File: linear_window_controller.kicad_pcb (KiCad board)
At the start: 4 copper layers, 114.3 x 86.4 mm, 148 parts, among them J1 Motor 2, J2 Motor 1, J3 Motor 4, J4 Motor 3, J5 Amphenol 10053363-200LF, J6 ATX-24 (Molex 39-28-1243), J7 Link-PP_LPJ0135GDNL, J8 EXT_LED, J9 Control, P1 ESP32 USB, P2 ESP32 USB, Q1 BC817-40(SOT23), Q2 BC817-40(SOT23), Q3 BSS138, SW1 PGM, SW2 Service, SW3 Service, SW4 Service, SW5 Service, SW7 Service, U1 TSOP384xx, U10 TPS56220x, U11 CP2102N-A01-GQFN24, U12 93LCxxAxxOT, U13 DM9051, U2 DRV8874, U3 DRV8874, U4 DRV8874, U5 DRV8874, U6 PCF8574APWRG4, U8 ESP32-S3-WROOM-1-N16R2, Y1 25MHz YXC X322525MOB4SI

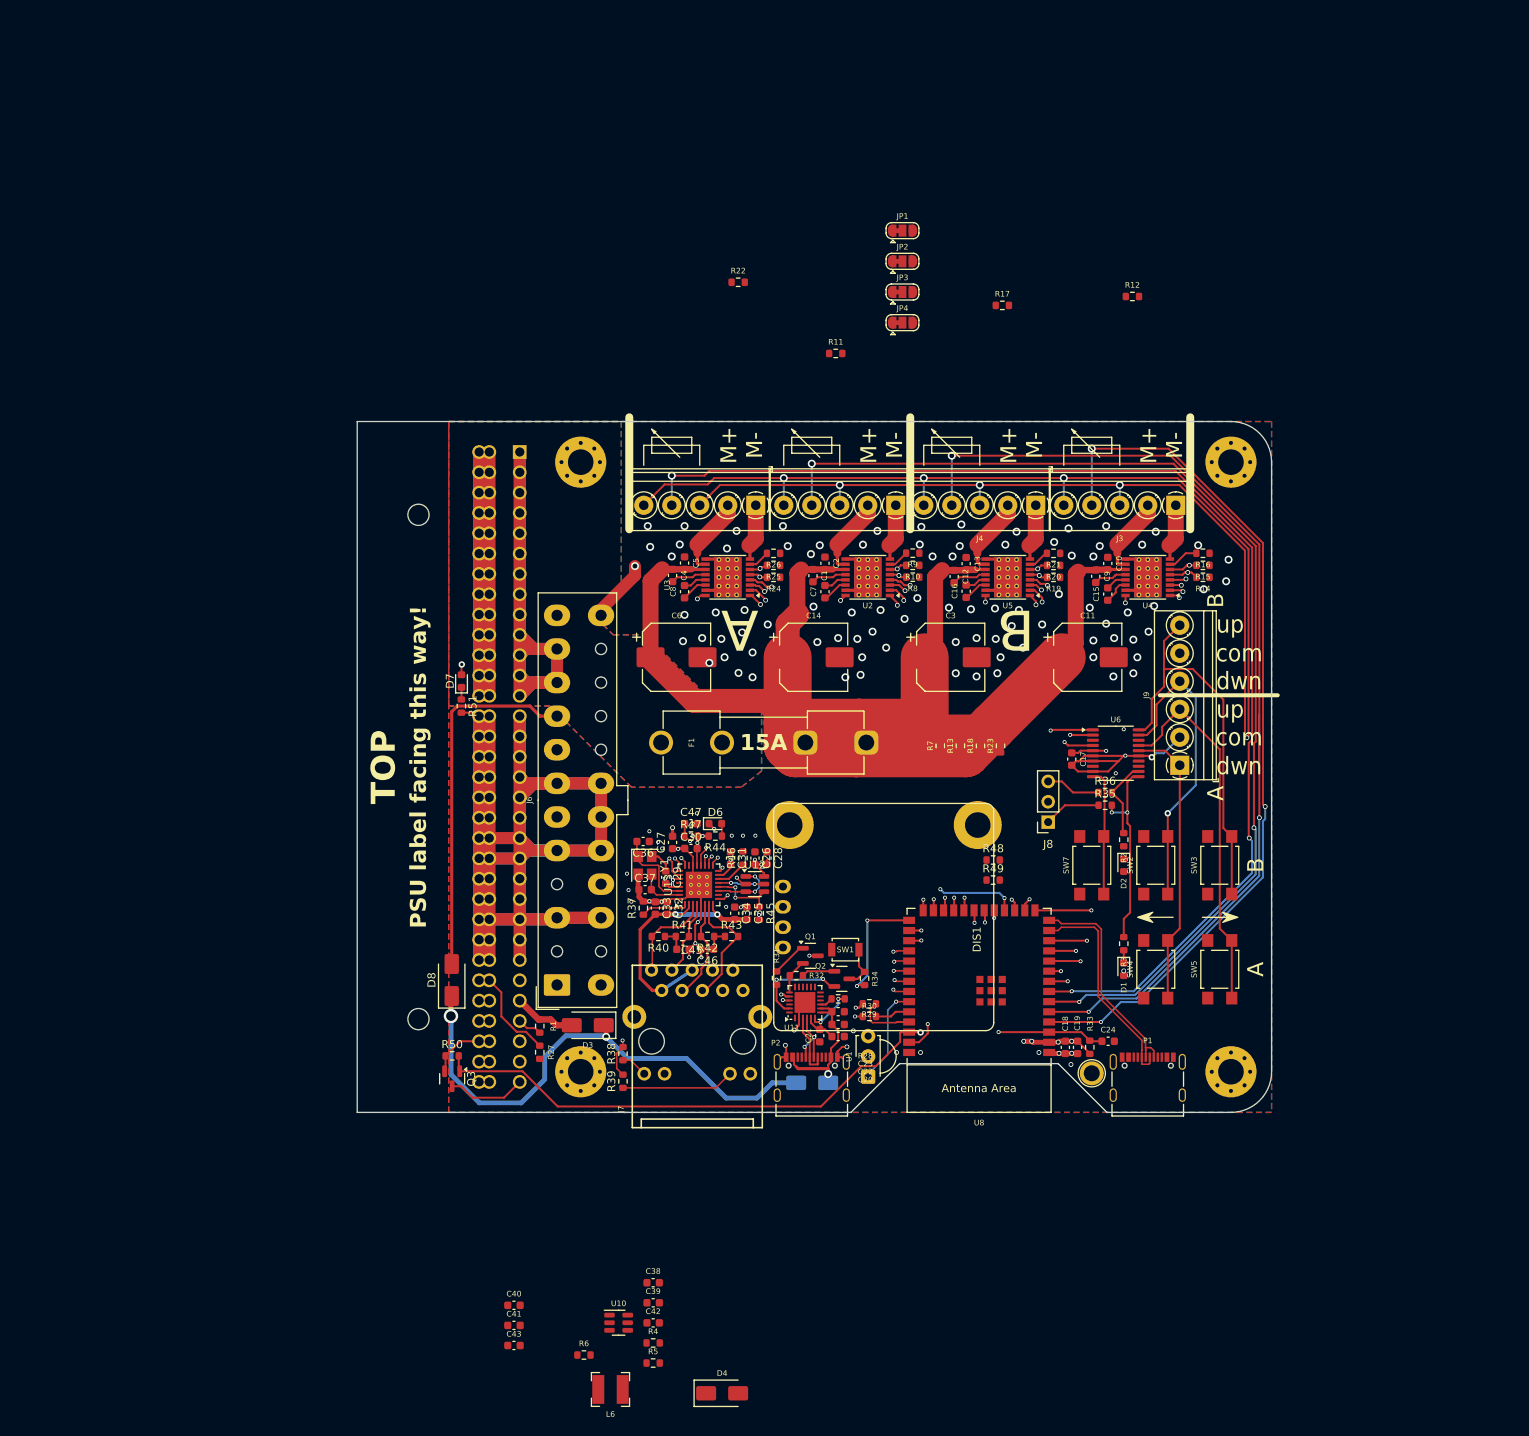
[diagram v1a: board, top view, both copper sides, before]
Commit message: Finalize routing and cleanup. Change DCDC to TPS562200 Add some more things (e.g. power monitoring LEDs) Update some partno's in BOM
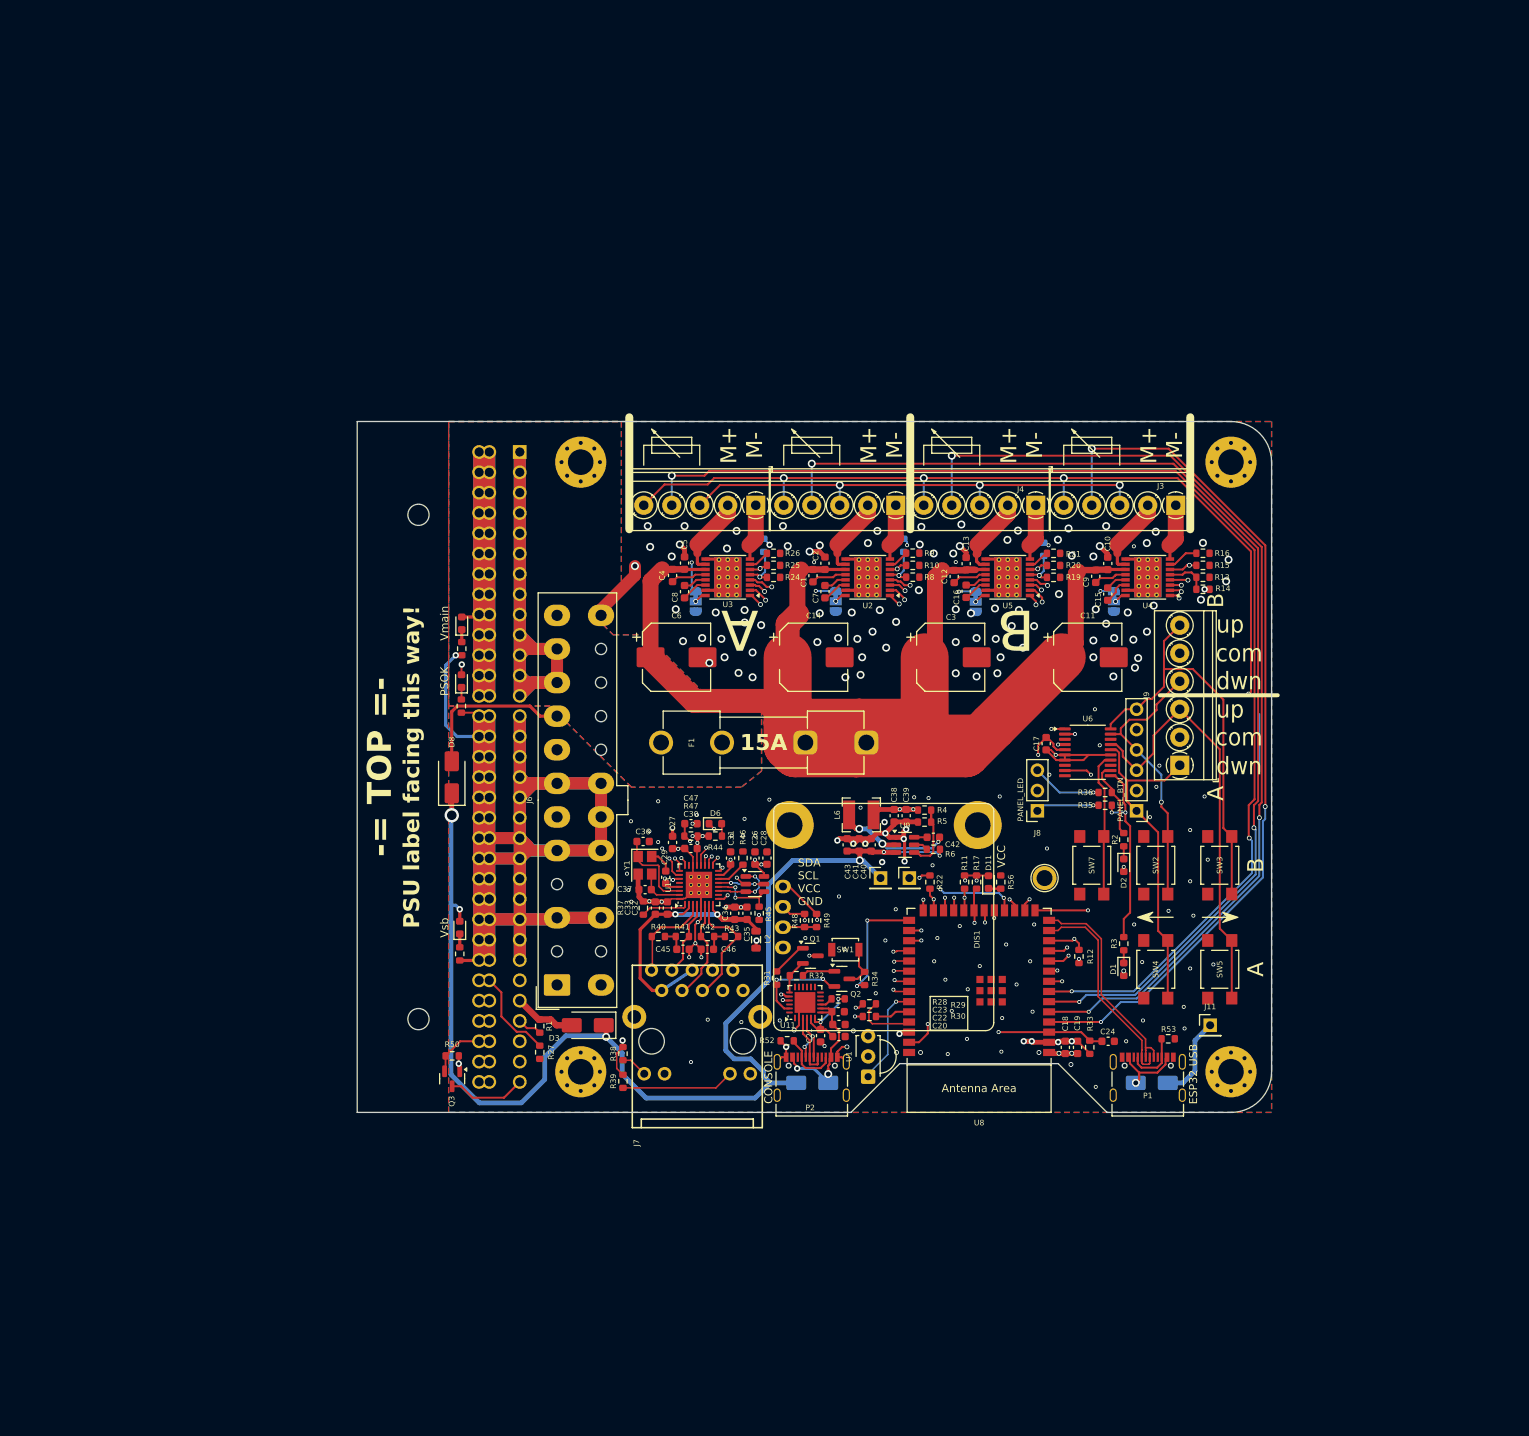
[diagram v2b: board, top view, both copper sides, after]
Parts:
- removed U10: TPS56220x, Package_TO_SOT_SMD:SOT-23-6
- added D10: Vsb, LED_SMD:LED_0603_1608Metric, F.Cu at (56.0, 112.8)
- added D11: VCC, LED_SMD:LED_0603_1608Metric, F.Cu at (122.1, 107.1)
- added D9: Vmain, LED_SMD:LED_0603_1608Metric, F.Cu at (56.2, 74.8)
- added J10: DCDC_IN, Connector_PinHeader_2.54mm:PinHeader_1x01_P2.54mm_Vertical, F.Cu at (108.6, 106.6)
- added J11: DCDC_IN, Connector_PinHeader_2.54mm:PinHeader_1x01_P2.54mm_Vertical, F.Cu at (149.8, 125.0)
- added J12: VCC, Connector_PinHeader_2.54mm:PinHeader_1x01_P2.54mm_Vertical, F.Cu at (112.2, 106.6)
- added J14: PANEL_BTN, Connector_PinHeader_2.54mm:PinHeader_1x06_P2.54mm_Vertical, F.Cu at (140.6, 98.2)
- added L2: FB0805/600R/2A, Inductor_SMD:L_0805_2012Metric, F.Cu at (93.0, 114.3)
- added R52: 1k, Resistor_SMD:R_0603_1608Metric, F.Cu at (96.9, 126.9)
- added R53: 1k, Resistor_SMD:R_0603_1608Metric, F.Cu at (144.6, 126.7)
- added R54: 300, Resistor_SMD:R_0603_1608Metric, F.Cu at (56.2, 77.9)
- added R55: 470, Resistor_SMD:R_0603_1608Metric, F.Cu at (56.0, 116.1)
- added R56: 100, Resistor_SMD:R_0603_1608Metric, F.Cu at (123.6, 107.1)
- added U9: TPS562200, Package_TO_SOT_SMD:SOT-23-6, F.Cu at (111.7, 102.5)
- C36, C37: value 100n -> 18p
- D4, JP1, JP2, JP3, JP4, R18, R23, R7: moved to B.Cu
- D7: value LED -> PSOK
- J8: value EXT_LED -> PANEL_LED
- L6: value 4.7µ -> 2.2µ
- P2: value ESP32 USB -> CONSOLE
- R4: value 100k -> 33k
- R5: value 22k -> 10k
- U12: value 93LCxxAxxOT -> 93LC46BT-E/OT
- moved R12 82.8 mm to (133.4, 116.4), turned to -90 degrees
- moved R22 78.7 mm to (114.8, 107.1), turned to 90 degrees
- moved L6 78.4 mm to (106.2, 98.7)
- moved R6 76.8 mm to (115.2, 103.0), turned to 180 degrees
- moved R5 75.7 mm to (114.1, 99.6)
- moved C43 75.2 mm to (104.4, 102.5), turned to -90 degrees
- moved R4 74.8 mm to (114.1, 98.1)
- moved C41 74.0 mm to (105.9, 102.5), turned to -90 degrees
- moved C40 72.8 mm to (107.4, 102.5), turned to -90 degrees
- moved R17 72.2 mm to (120.6, 107.1), turned to 90 degrees
- moved C42 70.1 mm to (115.2, 101.5)
- moved C39 68.6 mm to (111.8, 98.8), turned to 90 degrees
- moved R11 68.0 mm to (119.1, 107.1), turned to 90 degrees
- moved D4 66.3 mm to (142.5, 132.2), turned to 180 degrees
- moved C38 65.7 mm to (110.3, 98.8), turned to 90 degrees
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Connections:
- D4 pad 1: /DCDC_IN -> Net-(D4-K)
- J1 pad 3: /POTCOM -> GND
- J1 pad 5: /POT+ -> +3.3V
- J2 pad 3: /POTCOM -> GND
- J2 pad 5: /POT+ -> +3.3V
- J3 pad 3: /POTCOM -> GND
- J3 pad 5: /POT+ -> +3.3V
- J4 pad 3: /POTCOM -> GND
- J4 pad 5: /POT+ -> +3.3V
- J6 pad 1: /+3.3v -> unconnected-(J6-+3.3V-Pad1)_0
- J6 pad 12: /+3.3v -> unconnected-(J6-+3.3V-Pad1)_1
- J6 pad 13: /+3.3v -> unconnected-(J6-+3.3V-Pad1)
- J6 pad 6: /+5v -> unconnected-(J6-+5V-Pad21)
- P1 pad A5: unconnected-(P1-CC1-PadA5) -> Net-(P1-CC1)
- P1 pad B5: unconnected-(P1-CC2-PadB5) -> Net-(P1-CC1)
- P2 pad A5: unconnected-(P2-CC1-PadA5) -> Net-(P2-CC1)
- P2 pad B5: unconnected-(P2-CC2-PadB5) -> Net-(P2-CC1)
- U6 pad 10: /BTN_FUNC -> /BTN_SVC
- U6 pad 14: /BTN_SVC -> /BTN_FUNC
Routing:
- net +3.3V: track 61.8 -> 308.5 mm, vias 17 -> 40
- net /POT+: track 114.6 -> 0.00 mm, vias 4 -> 0
- net /POTCOM: track 102.9 -> 0.00 mm, vias 3 -> 0
- net GND: track 432.9 -> 529.7 mm, vias 122 -> 191
- net /DCDC_IN: track 65.2 -> 156.5 mm, vias 2 -> 6
- net /SCL: track 36.8 -> 73.7 mm, vias 2 -> 3
- net /SDA: track 34.4 -> 69.5 mm, vias 2 -> 3
- net Net-(U3-VRef): track 31.1 -> 5.51 mm
- net +5VSB: track 45.5 -> 20.2 mm
- net Net-(U4-VRef): track 28.2 -> 5.16 mm, vias 1 -> 0
- net Net-(U5-VRef): track 21.1 -> 4.94 mm
- net Net-(U9-SW): track 0.00 -> 15.3 mm, vias 0 -> 3
- net Net-(U2-VRef): track 20.1 -> 5.36 mm
- net Net-(D4-K): track 0.00 -> 10.5 mm
- net Net-(D4-A): track 0.00 -> 8.14 mm, vias 0 -> 1
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- added copper zone on In1.Cu, net GND
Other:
- board text added: "-= TOP =-"
- board text added: "SDA SCL VCC GND"
- board text removed: "TOP"

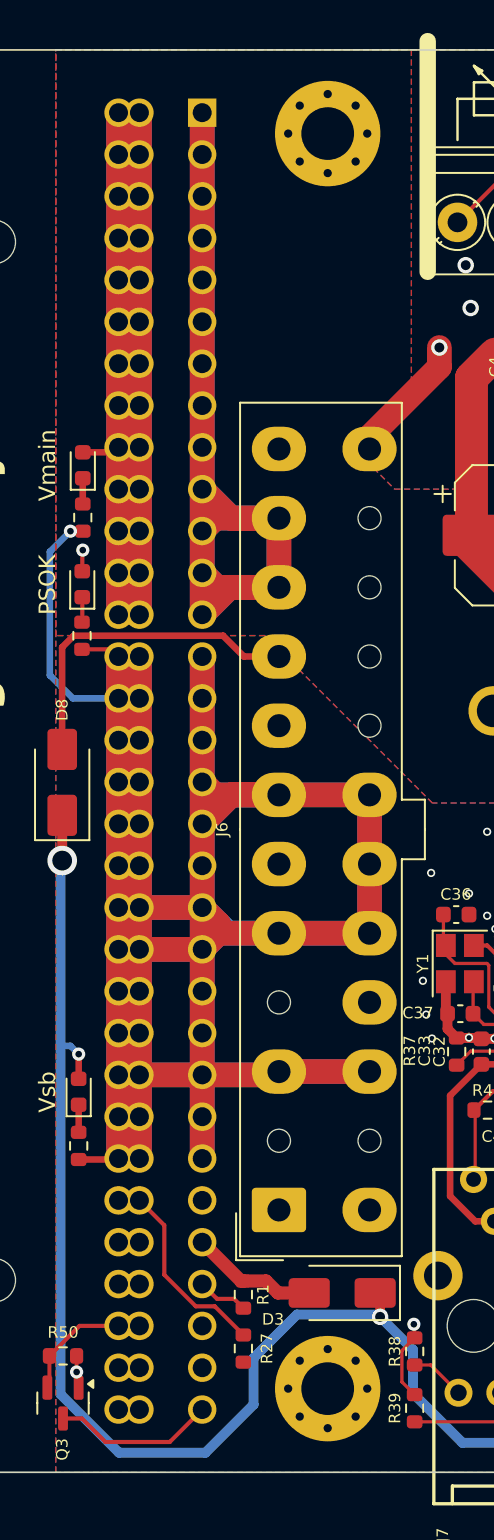
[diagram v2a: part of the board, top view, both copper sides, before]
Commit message: Update edge connector orientation (correct bottom mount)
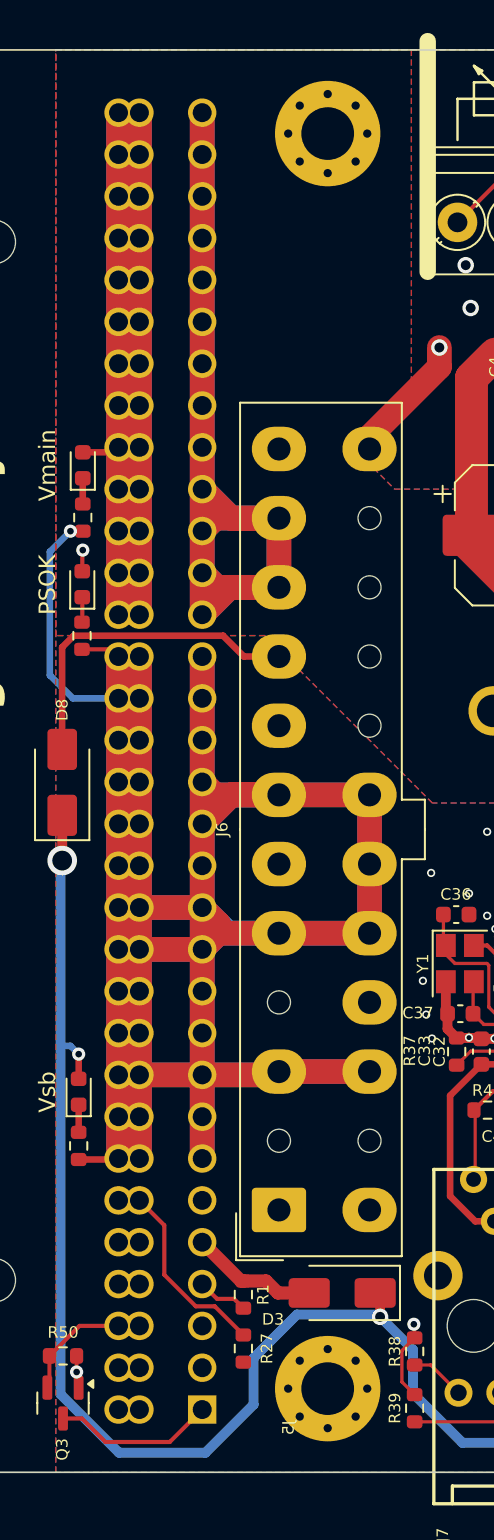
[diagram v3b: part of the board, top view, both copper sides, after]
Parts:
- J5: moved to B.Cu
- turned J5 to 90 degrees

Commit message: Add TMP100 and LIS3DH sensors, update board layout, teardrops
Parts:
- removed REF**: TestPoint_Plated_Hole_D2.0mm, TestPoint:TestPoint_Plated_Hole_D2.0mm
- added C25: 100n, Capacitor_SMD:C_0603_1608Metric, F.Cu at (101.3, 104.8)
- added C44: 100n, Capacitor_SMD:C_0603_1608Metric, F.Cu at (108.5, 77.9)
- added H5: 12V MAIN, MountingHole:MountingHole_3.2mm_M3_Pad_Via, F.Cu at (71.1, 64.9)
- added J13: GND, TestPoint:TestPoint_Plated_Hole_D2.0mm, F.Cu at (129.2, 103.8)
- added Q4: BSS138, Package_TO_SOT_SMD:SOT-23, F.Cu at (132.1, 96.7)
- added R57: 10k, Resistor_SMD:R_0603_1608Metric, F.Cu at (131.9, 99.4)
- added U10: TMP100, Package_TO_SOT_SMD:SOT-23-6, F.Cu at (108.4, 80.6)
- added U7: LIS3DH, Package_LGA:LGA-16_3x3mm_P0.5mm_LayoutBorder3x5y, F.Cu at (101.6, 107.8)
- C38, C39: value 22µ -> 22u
- C41, C43: value 10µ -> 10u
- H4: value MountingHole -> GND
- J11: value DCDC_IN -> VBus
- moved D10 44.4 mm to (55.5, 68.3)
- moved R55 44.4 mm to (55.5, 71.6)
- moved R27 18.2 mm to (55.5, 113.5), turned to 90 degrees
- moved D3 17.7 mm to (55.0, 120.1), turned to -90 degrees
- moved R1 10.5 mm to (55.5, 125.5)
- moved D7 1.13 mm to (55.5, 81.1)
- moved R51 1.12 mm to (55.5, 84.2)
- moved D9 0.75 mm to (55.5, 74.8)
- moved R54 0.75 mm to (55.5, 77.9)
- moved R49 0.50 mm to (101.1, 111.9)
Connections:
- H4 pad 1: (no net) -> GND
- J5 pad A27: Net-(J5-ADDR) -> /PS_INTERRUPT
- J5 pad A28: unconnected-(J5-Reserved-PadA28) -> +V12SB
- J5 pad A29: unconnected-(J5-Reserved-PadA29) -> Net-(J5-PRESENT#)
- J5 pad A30: GND -> /PS_OK
- J5 pad A31: /PS_SDA -> /PS_IMONITOR
- J5 pad A32: /PS_SCL -> /PS_ON
- J5 pad B27: /PS_INTERRUPT -> Net-(J5-ADDR)
- J5 pad B28: +V12SB -> unconnected-(J5-Reserved-PadB28)
- J5 pad B29: Net-(J5-PRESENT#) -> unconnected-(J5-Reserved-PadB29)
- J5 pad B30: /PS_OK -> GND
- J5 pad B31: /PS_IMONITOR -> /PS_SDA
- J5 pad B32: /PS_ON -> /PS_SCL
- U6 pad 10: /BTN_SVC -> /~{nPS_OK}
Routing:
- net /PS_OK: track 63.0 -> 132.8 mm, vias 1 -> 3
- net /SDA: track 69.5 -> 102.4 mm, vias 3 -> 4
- net +3.3V: track 308.5 -> 340.4 mm
- net /SCL: track 73.7 -> 104.2 mm, vias 3 -> 4
- net /DCDC_IN: track 156.5 -> 181.7 mm, vias 6 -> 7
- net GND: track 529.7 -> 547.2 mm, vias 191 -> 202
- net +5VSB: track 20.2 -> 33.2 mm, vias 0 -> 1
- net /PS_ON: track 38.8 -> 36.2 mm
- net +V12SB: track 7.78 -> 5.41 mm
- net /~{nPS_OK}: track 0.00 -> 2.09 mm
- net /+12V_UNFUSED: track 234.6 -> 232.8 mm, vias 0 -> 25
- net Net-(J8-Pin_1): track 7.94 -> 6.95 mm
- net /LAN_CSN: track 32.5 -> 33.4 mm
- net /LAN_MISO: track 34.3 -> 35.1 mm
- net /LAN_CK: track 33.0 -> 33.9 mm
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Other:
- board text added: "2x2 Quad Motor Controller (c) 2024 iotta"
